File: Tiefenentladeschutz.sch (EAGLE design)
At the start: 23 parts, among them IC1 ICL7665CSA, Q4 NMOSFET-D2PAK-7

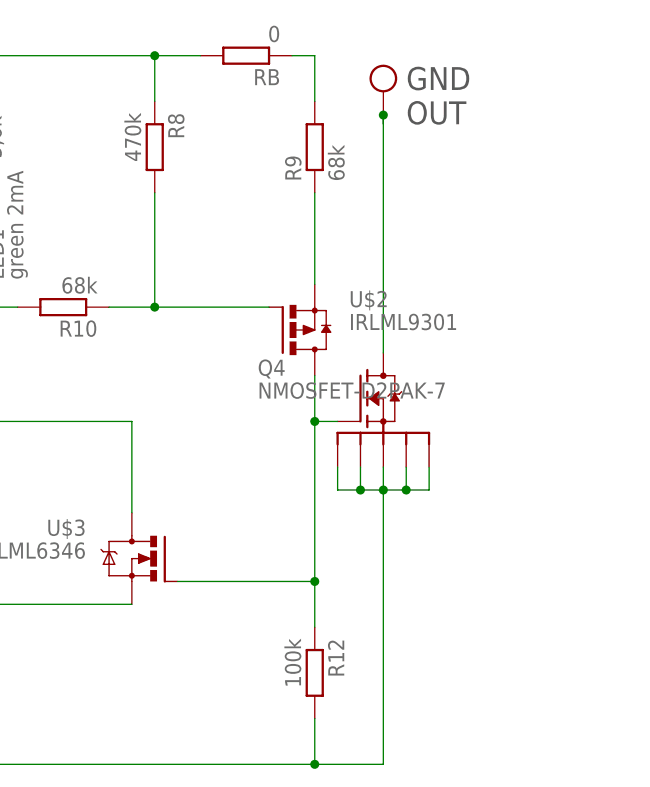
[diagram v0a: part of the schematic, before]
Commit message: Added Mosfet Gate Resistors
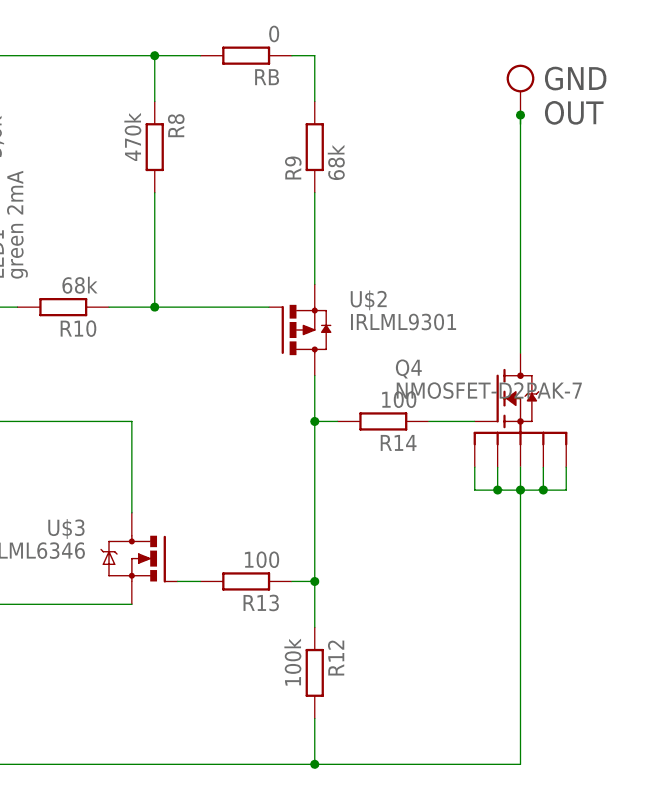
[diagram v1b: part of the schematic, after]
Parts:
- added R13, R14: 100, eagle-ltspice:RR1206
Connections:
- new net N$12: Q4.G, R14.1
- new net N$9: R13.2, U$3.G
- net N$22: now also R13.1, R14.2; no longer Q4.G, U$3.G
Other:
- moved on the sheet: Q4
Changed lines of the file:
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@@
 <grid distance="0.1" unitdist="inch" unit="inch" style="lines" multiple="1" display="no" altdistance="0.01" altunitdist="inch" altunit="inch"/>
 <layers>
-<layer number="1" name="Top" color="4" fill="1" visible="yes" active="no"/>
-<layer number="16" name="Bottom" color="1" fill="1" visible="yes" active="no"/>
-<layer number="17" name="Pads" color="2" fill="1" visible="yes" active="no"/>
-<layer number="18" name="Vias" color="2" fill="1" visible="yes" active="no"/>
-<layer number="19" name="Unrouted" color="6" fill="1" visible="yes" active="no"/>
-<layer number="20" name="Dimension" color="15" fill="1" visible="yes" active="no"/>
-<layer number="21" name="tPlace" color="7" fill="1" visible="yes" active="no"/>
-<layer number="22" name="bPlace" color="7" fill="1" visible="yes" active="no"/>
-<layer number="23" name="tOrigins" color="15" fill="1" visible="yes" active="no"/>
-<layer number="24" name="bOrigins" color="15" fill="1" visible="yes" active="no"/>
-<layer number="25" name="tNames" color="7" fill="1" visible="yes" active="no"/>
-<layer number="26" name="bNames" color="7" fill="1" visible="yes" active="no"/>
-<layer number="27" name="tValues" color="7" fill="1" visible="yes" active="no"/>
-<layer number="28" name="bValues" color="7" fill="1" visible="yes" active="no"/>
+<layer number="1" name="Top" color="4" fill="1" visible="no" active="no"/>
+<layer number="16" name="Bottom" color="1" fill="1" visible="no" active="no"/>
+<layer number="17" name="Pads" color="2" fill="1" visible="no" active="no"/>
+<layer number="18" name="Vias" color="2" fill="1" visible="no" active="no"/>
+<layer number="19" name="Unrouted" color="6" fill="1" visible="no" active="no"/>
+<layer number="20" name="Dimension" color="15" fill="1" visible="no" active="no"/>
+<layer number="21" name="tPlace" color="7" fill="1" visible="no" active="no"/>
+<layer number="22" name="bPlace" color="7" fill="1" visible="no" active="no"/>
+<layer number="23" name="tOrigins" color="15" fill="1" visible="no" active="no"/>
+<layer number="24" name="bOrigins" color="15" fill="1" visible="no" active="no"/>
+<layer number="25" name="tNames" color="7" fill="1" visible="no" active="no"/>
+<layer number="26" name="bNames" color="7" fill="1" visible="no" active="no"/>
+<layer number="27" name="tValues" color="7" fill="1" visible="no" active="no"/>
+<layer number="28" name="bValues" color="7" fill="1" visible="no" active="no"/>
 <layer number="29" name="tStop" color="7" fill="3" visible="no" active="no"/>
 <layer number="30" name="bStop" color="7" fill="6" visible="no" active="no"/>
@@
 <layer number="35" name="tGlue" color="7" fill="4" visible="no" active="no"/>
 <layer number="36" name="bGlue" color="7" fill="5" visible="no" active="no"/>
-<layer number="37" name="tTest" color="7" fill="1" visible="yes" active="no"/>
-<layer number="38" name="bTest" color="7" fill="1" visible="yes" active="no"/>
+<layer number="37" name="tTest" color="7" fill="1" visible="no" active="no"/>
+<layer number="38" name="bTest" color="7" fill="1" visible="no" active="no"/>
 <layer number="39" name="tKeepout" color="4" fill="11" visible="no" active="no"/>
 <layer number="40" name="bKeepout" color="1" fill="11" visible="no" active="no"/>
@@
 <layer number="44" name="Drills" color="7" fill="1" visible="no" active="no"/>
 <layer number="45" name="Holes" color="7" fill="1" visible="no" active="no"/>
-<layer number="46" name="Milling" color="3" fill="1" visible="yes" active="no"/>
-<layer number="47" name="Measures" color="7" fill="1" visible="yes" active="no"/>
-<layer number="48" name="Document" color="7" fill="1" visible="yes" active="no"/>
-<layer number="49" name="Reference" color="7" fill="1" visible="yes" active="no"/>
-<layer number="51" name="tDocu" color="7" fill="1" visible="yes" active="no"/>
-<layer number="52" name="bDocu" color="7" fill="1" visible="yes" active="no"/>
+<layer number="46" name="Milling" color="3" fill="1" visible="no" active="no"/>
+<layer number="47" name="Measures" color="7" fill="1" visible="no" active="no"/>
+<layer number="48" name="Document" color="7" fill="1" visible="no" active="no"/>
+<layer number="49" name="Reference" color="7" fill="1" visible="no" active="no"/>
+<layer number="51" name="tDocu" color="7" fill="1" visible="no" active="no"/>
+<layer number="52" name="bDocu" color="7" fill="1" visible="no" active="no"/>
 <layer number="90" name="Modules" color="5" fill="1" visible="yes" active="yes"/>
 <layer number="91" name="Nets" color="2" fill="1" visible="yes" active="yes"/>
@@
 <part name="RB" library="eagle-ltspice" deviceset="R" device="R1206" value="0"/>
 <part name="Q4" library="D2pak-7" deviceset="NMOSFET-D2PAK-7" device=""/>
+<part name="R13" library="eagle-ltspice" deviceset="R" device="R1206" value="100"/>
+<part name="R14" library="eagle-ltspice" deviceset="R" device="R1206" value="100"/>
 </parts>
 <sheets>
@@
 <plain>
 <text x="-32.512" y="59.182" size="2.54" layer="97">+</text>
-<text x="114.3" y="88.9" size="2.54" layer="97">GND
+<text x="129.54" y="88.9" size="2.54" layer="97">GND
 OUT</text>
 </plain>
@@
 <instance part="U$4" gate="G$1" x="-33.02" y="58.42" rot="R90"/>
 <instance part="U$6" gate="G$1" x="-33.02" y="53.34" rot="R90"/>
-<instance part="U$7" gate="G$1" x="111.76" y="93.98"/>
+<instance part="U$7" gate="G$1" x="127" y="93.98"/>
 <instance part="RB" gate="G$1" x="96.52" y="96.52" rot="R180"/>
-<instance part="Q4" gate="G$1" x="109.22" y="58.42"/>
+<instance part="Q4" gate="G$1" x="124.46" y="58.42"/>
+<instance part="R13" gate="G$1" x="96.52" y="38.1" rot="R180"/>
+<instance part="R14" gate="G$1" x="111.76" y="55.88" rot="R180"/>
 </instances>
 <busses>
@@
 <pinref part="R12" gate="G$1" pin="2"/>
 <wire x1="104.14" y1="17.78" x2="104.14" y2="22.86" width="0.1524" layer="91"/>
-<wire x1="106.68" y1="48.26" x2="109.22" y2="48.26" width="0.1524" layer="91"/>
-<wire x1="109.22" y1="48.26" x2="111.76" y2="48.26" width="0.1524" layer="91"/>
-<wire x1="111.76" y1="48.26" x2="114.3" y2="48.26" width="0.1524" layer="91"/>
-<wire x1="114.3" y1="48.26" x2="116.84" y2="48.26" width="0.1524" layer="91"/>
-<junction x="111.76" y="48.26"/>
-<junction x="114.3" y="48.26"/>
-<junction x="109.22" y="48.26"/>
-<wire x1="111.76" y1="48.26" x2="111.76" y2="17.78" width="0.1524" layer="91"/>
-<wire x1="111.76" y1="17.78" x2="104.14" y2="17.78" width="0.1524" layer="91"/>
+<wire x1="121.92" y1="48.26" x2="124.46" y2="48.26" width="0.1524" layer="91"/>
+<wire x1="124.46" y1="48.26" x2="127" y2="48.26" width="0.1524" layer="91"/>
+<wire x1="127" y1="48.26" x2="129.54" y2="48.26" width="0.1524" layer="91"/>
+<wire x1="129.54" y1="48.26" x2="132.08" y2="48.26" width="0.1524" layer="91"/>
+<junction x="127" y="48.26"/>
+<junction x="129.54" y="48.26"/>
+<junction x="124.46" y="48.26"/>
+<wire x1="127" y1="48.26" x2="127" y2="17.78" width="0.1524" layer="91"/>
+<wire x1="127" y1="17.78" x2="104.14" y2="17.78" width="0.1524" layer="91"/>
 <junction x="104.14" y="17.78"/>
 <wire x1="-30.48" y1="53.34" x2="-28.96" y2="53.34" width="0.1524" layer="91"/>
@@
 <pinref part="Q4" gate="G$1" pin="S4"/>
 <pinref part="Q4" gate="G$1" pin="S5"/>
-<wire x1="106.68" y1="48.26" x2="106.68" y2="50.8" width="0.1524" layer="91"/>
-<wire x1="109.22" y1="48.26" x2="109.22" y2="50.8" width="0.1524" layer="91"/>
-<wire x1="116.84" y1="48.26" x2="116.84" y2="50.8" width="0.1524" layer="91"/>
-<wire x1="111.76" y1="48.26" x2="111.76" y2="50.8" width="0.1524" layer="91"/>
-<wire x1="114.3" y1="48.26" x2="114.3" y2="50.8" width="0.1524" layer="91"/>
+<wire x1="121.92" y1="48.26" x2="121.92" y2="50.8" width="0.1524" layer="91"/>
+<wire x1="124.46" y1="48.26" x2="124.46" y2="50.8" width="0.1524" layer="91"/>
+<wire x1="132.08" y1="48.26" x2="132.08" y2="50.8" width="0.1524" layer="91"/>
+<wire x1="127" y1="48.26" x2="127" y2="50.8" width="0.1524" layer="91"/>
+<wire x1="129.54" y1="48.26" x2="129.54" y2="50.8" width="0.1524" layer="91"/>
 </segment>
 </net>
@@
 <junction x="104.14" y="55.88"/>
 <wire x1="104.14" y1="38.1" x2="104.14" y2="55.88" width="0.1524" layer="91"/>
-<wire x1="104.14" y1="38.1" x2="88.9" y2="38.1" width="0.1524" layer="91"/>
+<wire x1="104.14" y1="38.1" x2="101.6" y2="38.1" width="0.1524" layer="91"/>
 <junction x="104.14" y="38.1"/>
 <wire x1="104.14" y1="60.96" x2="104.14" y2="55.88" width="0.1524" layer="91"/>
-<pinref part="U$3" gate="G$1" pin="G"/>
 <pinref part="U$2" gate="G$1" pin="D"/>
-<pinref part="Q4" gate="G$1" pin="G"/>
 <wire x1="104.14" y1="55.88" x2="106.68" y2="55.88" width="0.1524" layer="91"/>
+<pinref part="R13" gate="G$1" pin="1"/>
+<pinref part="R14" gate="G$1" pin="2"/>
 </segment>
 </net>
@@
 <net name="N$1" class="0">
 <segment>
-<wire x1="111.76" y1="63.5" x2="111.76" y2="89.92" width="0.1524" layer="91"/>
+<wire x1="127" y1="63.5" x2="127" y2="89.92" width="0.1524" layer="91"/>
 <pinref part="U$7" gate="G$1" pin="P$1"/>
-<wire x1="111.76" y1="89.92" x2="111.76" y2="88.9" width="0.1524" layer="91"/>
-<junction x="111.76" y="89.92"/>
+<wire x1="127" y1="89.92" x2="127" y2="88.9" width="0.1524" layer="91"/>
+<junction x="127" y="89.92"/>
 <pinref part="Q4" gate="G$1" pin="D"/>
 </segment>
@@
 </segment>
 </net>
+<net name="N$9" class="0">
+<segment>
+<pinref part="R13" gate="G$1" pin="2"/>
+<wire x1="91.44" y1="38.1" x2="88.9" y2="38.1" width="0.1524" layer="91"/>
+<pinref part="U$3" gate="G$1" pin="G"/>
+</segment>
+</net>
+<net name="N$12" class="0">
+<segment>
+<pinref part="Q4" gate="G$1" pin="G"/>
+<pinref part="R14" gate="G$1" pin="1"/>
+<wire x1="116.84" y1="55.88" x2="121.92" y2="55.88" width="0.1524" layer="91"/>
+</segment>
+</net>
